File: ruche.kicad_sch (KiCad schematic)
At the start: 36 parts, among them IC2 MAX17048G+, IC3 L86-M33, IC4 SHT41-AD1B-R3, J13 Micro_SD_Card, U1 MKRWAN_1310, U2 MS5611-01BA, U3 XC6220B331MR

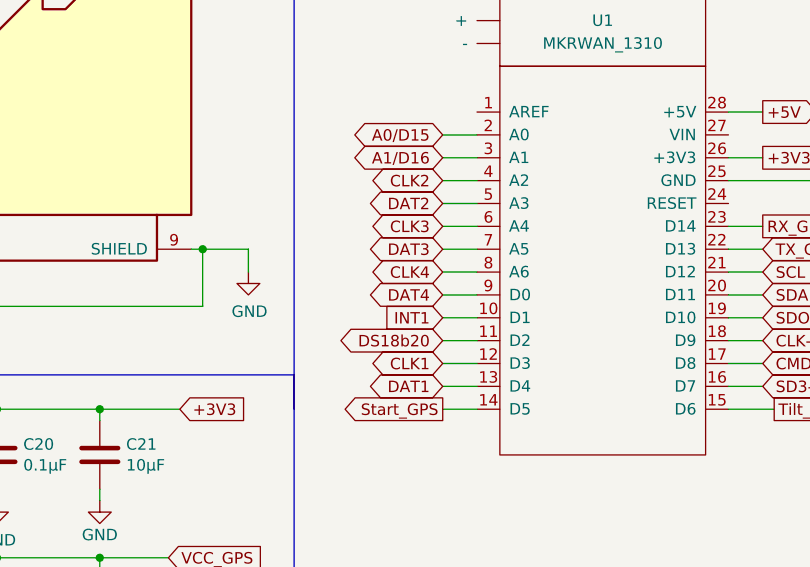
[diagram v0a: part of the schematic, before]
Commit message: Added HX711
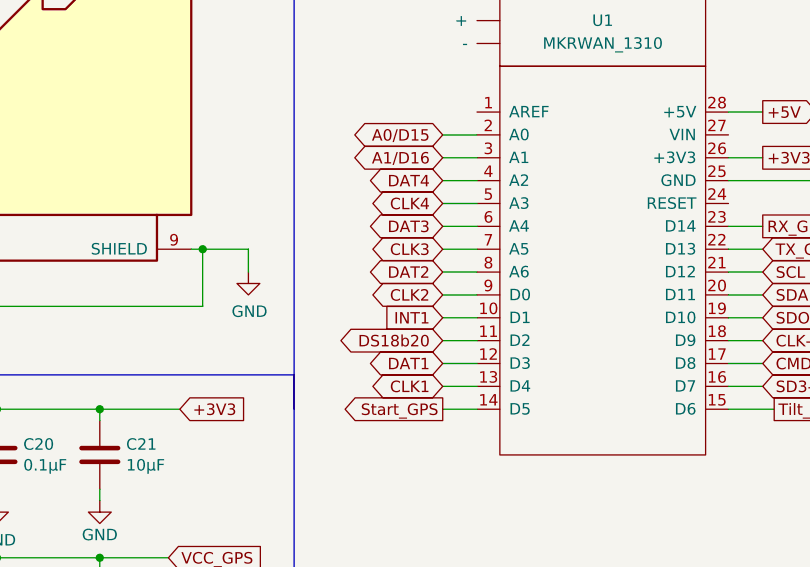
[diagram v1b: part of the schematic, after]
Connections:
- net CLK1: now also U1.13 (D4); no longer U1.12 (D3)
- net CLK2: now also U1.9 (D0); no longer U1.4 (A2)
- net CLK3: now also U1.7 (A5); no longer U1.6 (A4)
- net CLK4: now also U1.5 (A3); no longer U1.8 (A6)
- net DAT1: now also U1.12 (D3); no longer U1.13 (D4)
- net DAT2: now also U1.8 (A6); no longer U1.5 (A3)
- net DAT3: now also U1.6 (A4); no longer U1.7 (A5)
- net DAT4: now also U1.4 (A2); no longer U1.9 (D0)

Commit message: update
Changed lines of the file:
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@@
   (junction (at 53.34 72.39) (diameter 0) (color 0 0 0 0)
   )
-  (junction (at 191.77 91.44) (diameter 0) (color 0 0 0 0)
-  )
   (junction (at 220.98 78.74) (diameter 0) (color 0 0 0 0)
   )
@@
     (stroke (width 0) (type default) (color 0 0 0 0))
   )
+  (wire (pts (xy 191.77 88.9) (xy 191.77 93.98))
+    (stroke (width 0) (type default) (color 0 0 0 0))
+  )
   (wire (pts (xy 113.03 96.52) (xy 118.11 96.52))
     (stroke (width 0) (type default) (color 0 0 0 0))
@@
   )
   (wire (pts (xy 30.48 88.9) (xy 68.58 88.9))
-    (stroke (width 0) (type default) (color 0 0 0 0))
-  )
-  (wire (pts (xy 191.77 88.9) (xy 191.77 91.44))
     (stroke (width 0) (type default) (color 0 0 0 0))
   )
@@
     (pin "1")
   )
-  (symbol (lib_id "power:GND") (at 191.77 91.44 0) (unit 1)
-    (in_bom yes) (on_board yes)
-    (property "Reference" "#PWR0124" (id 0) (at 191.77 97.79 0)
-      (effects (font (size 1.27 1.27)) hide)
-    )
-    (property "Value" "GND" (id 1) (at 191.897 95.8342 0))
-    (property "Footprint" "" (id 2) (at 191.77 91.44 0)
-      (effects (font (size 1.27 1.27)) hide)
-    )
-    (property "Datasheet" "" (id 3) (at 191.77 91.44 0)
-      (effects (font (size 1.27 1.27)) hide)
-    )
-    (pin "1")
-  )
-  (symbol (lib_id "power:GND") (at 191.77 91.44 0) (unit 1)
-    (in_bom yes) (on_board yes)
-    (property "Reference" "#PWR0125" (id 0) (at 191.77 97.79 0)
-      (effects (font (size 1.27 1.27)) hide)
-    )
-    (property "Value" "GND" (id 1) (at 191.897 95.8342 0))
-    (property "Footprint" "" (id 2) (at 191.77 91.44 0)
-      (effects (font (size 1.27 1.27)) hide)
-    )
-    (property "Datasheet" "" (id 3) (at 191.77 91.44 0)
+  (symbol (lib_id "power:GND") (at 191.77 93.98 0) (unit 1)
+    (in_bom yes) (on_board yes)
+    (property "Reference" "#PWR0125" (id 0) (at 191.77 100.33 0)
+      (effects (font (size 1.27 1.27)) hide)
+    )
+    (property "Value" "GND" (id 1) (at 191.897 98.3742 0))
+    (property "Footprint" "" (id 2) (at 191.77 93.98 0)
+      (effects (font (size 1.27 1.27)) hide)
+    )
+    (property "Datasheet" "" (id 3) (at 191.77 93.98 0)
       (effects (font (size 1.27 1.27)) hide)
     )
@@
       (reference "#PWR0123") (unit 1) (value "GND") (footprint "")
     )
-    (path "/00000000-0000-0000-0000-000062832503"
-      (reference "#PWR0124") (unit 1) (value "GND") (footprint "")
-    )
     (path "/00000000-0000-0000-0000-000062832ae7"

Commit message: Update
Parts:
- added C51: 10µF, Capacitor_SMD:C_0603_1608Metric, symbol Device:C
- added C52: 0.1µF, Capacitor_SMD:C_0805_2012Metric, symbol Device:C
- added C53: 0.1µF, Capacitor_SMD:C_0603_1608Metric, symbol Device:C
- added C54: 10µF, Capacitor_SMD:C_0805_2012Metric, symbol Device:C
- added R41: 10K, Resistor_SMD:R_0603_1608Metric, symbol Device:R
- added U5: XC6220B331MR, Package_TO_SOT_SMD:SOT-23-5, symbol Regulator_Linear:XC6220B331MR
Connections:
- net +3V3: no longer C10.1, C12.1, C19.1, FB1.2, IC4.3 (VDD), J13.4 (VDD), R13.1, R14.1, R15.1
- net GND: now also C51.2, C52.2, C53.2, C54.2, U5.2 (GND)
- net VBAT: now also C51.1, C52.1, U5.1 (VIN)
- net A1/D16 renamed Start_modules
- net Start_modules: now also R41.2
- new net: R41.1, U5.3 (CE)
- new net VCC: C10.1, C12.1, C19.1, C53.1, C54.1, FB1.2, IC4.3 (VDD), J13.4 (VDD), R13.1, R14.1, R15.1, U5.5 (VOUT)
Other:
- note added: "Modules POWER SUPPLY"
- moved on the sheet: C15, C16, C17, C18, C5, FID1, FID2, FID3, FID4, IC2, R12, U1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

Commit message: Ajouté code
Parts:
- removed R12, R41: 10K, Resistor_SMD:R_0603_1608Metric, symbol Device:R
- added J19: Conn_01x02, Connector_JST:JST_PH_B2B-PH-K_1x02_P2.00mm_Vertical, symbol Connector_Generic:Conn_01x02
- C21: value 10µF -> 4.7µF
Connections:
- net GND: now also J19.2 (Pin_2)
- net Start_GPS: now also U3.3 (CE)
- net Start_modules: now also U5.3 (CE)
- net Reset-button: now reaches U1.24 (RESET)
- net Reset-button: now also J19.1 (Pin_1)
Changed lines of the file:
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@@
     (stroke (width 0) (type default) (color 0 0 0 0))
   )
+  (wire (pts (xy 146.05 176.53) (xy 146.05 182.88))
+    (stroke (width 0) (type default) (color 0 0 0 0))
+  )
   (wire (pts (xy 45.72 172.72) (xy 45.72 167.64))
     (stroke (width 0) (type default) (color 0 0 0 0))
@@
     (stroke (width 0) (type default) (color 0 0 0 0))
   )
-  (wire (pts (xy 55.88 29.21) (xy 54.61 29.21))
+  (wire (pts (xy 54.61 29.21) (xy 63.5 29.21))
     (stroke (width 0) (type default) (color 0 0 0 0))
   )
@@
     (stroke (width 0) (type default) (color 0 0 0 0))
   )
+  (wire (pts (xy 140.97 173.99) (xy 153.67 173.99))
+    (stroke (width 0) (type default) (color 0 0 0 0))
+  )
   (wire (pts (xy 266.7 105.41) (xy 266.7 106.68))
     (stroke (width 0) (type default) (color 0 0 0 0))
@@
     (stroke (width 0) (type default) (color 0 0 0 0))
   )
+  (wire (pts (xy 172.72 49.53) (xy 176.53 49.53))
+    (stroke (width 0) (type default) (color 0 0 0 0))
+  )
   (wire (pts (xy 88.9 167.64) (xy 91.44 167.64))
     (stroke (width 0) (type default) (color 0 0 0 0))
@@
     (stroke (width 0) (type default) (color 0 0 0 0))
   )
+  (wire (pts (xy 153.67 176.53) (xy 146.05 176.53))
+    (stroke (width 0) (type default) (color 0 0 0 0))
+  )
   (wire (pts (xy 30.48 162.56) (xy 49.53 162.56))
     (stroke (width 0) (type default) (color 0 0 0 0))
@@
     (stroke (width 0) (type default) (color 0 0 0 0))
   )
-  (wire (pts (xy 53.34 172.72) (xy 49.53 172.72))
-    (stroke (width 0) (type default) (color 0 0 0 0))
-  )
-  (wire (pts (xy 60.96 172.72) (xy 63.5 172.72))
+  (wire (pts (xy 49.53 172.72) (xy 63.5 172.72))
     (stroke (width 0) (type default) (color 0 0 0 0))
   )
@@
     )
   )
+  (global_label "Reset-button" (shape input) (at 140.97 173.99 180) (fields_autoplaced)
+    (effects (font (size 1.27 1.27)) (justify right))
+    (property "Intersheet References" "${INTERSHEET_REFS}" (id 0) (at 125.8248 173.9106 0)
+      (effects (font (size 1.27 1.27)) (justify right) hide)
+    )
+  )
   (global_label "+3V3" (shape input) (at 110.49 114.3 0) (fields_autoplaced)
     (effects (font (size 1.27 1.27)) (justify left))
@@
     )
   )
+  (global_label "Reset-button" (shape output) (at 176.53 49.53 0) (fields_autoplaced)
+    (effects (font (size 1.27 1.27)) (justify left))
+    (property "Intersheet References" "${INTERSHEET_REFS}" (id 0) (at 191.6752 49.4506 0)
+      (effects (font (size 1.27 1.27)) (justify left) hide)
+    )
+  )
   (global_label "DAT1" (shape bidirectional) (at 140.97 67.31 180) (fields_autoplaced)
     (effects (font (size 1.27 1.27)) (justify right))
@@
     )
   )
-  (symbol (lib_id "Device:R") (at 59.69 29.21 270) (unit 1)
+  (symbol (lib_id "power:GND") (at 146.05 182.88 0) (unit 1)
     (in_bom yes) (on_board yes)
-    (property "Reference" "R41" (id 0) (at 59.69 22.6822 90))
-    (property "Value" "10K" (id 1) (at 59.69 26.2636 90))
-    (property "Footprint" "Resistor_SMD:R_0603_1608Metric" (id 2) (at 59.69 27.432 90)
+    (property "Reference" "#PWR0202" (id 0) (at 146.05 189.23 0)
+      (effects (font (size 1.27 1.27)) hide)
+    )
+    (property "Value" "GND" (id 1) (at 146.177 187.2742 0))
+    (property "Footprint" "" (id 2) (at 146.05 182.88 0)
       (effects (font (size 1.27 1.27)) hide)
     )
-    (property "Datasheet" "~" (id 3) (at 59.69 29.21 0)
+    (property "Datasheet" "" (id 3) (at 146.05 182.88 0)
       (effects (font (size 1.27 1.27)) hide)
     )
     (pin "1")
-    (pin "2")
   )
   (symbol (lib_id "Device:C") (at 232.41 83.82 0) (unit 1)
@@
       (effects (font (size 1.27 1.27)) (justify left))
     )
-    (property "Value" "10µF" (id 1) (at 104.521 120.523 0)
+    (property "Value" "4.7µF" (id 1) (at 104.521 120.523 0)
       (effects (font (size 1.27 1.27)) (justify left))
     )
@@
     (pin "2")
   )
-  (symbol (lib_id "Device:R") (at 57.15 172.72 270) (unit 1)
-    (in_bom yes) (on_board yes)
-    (property "Reference" "R12" (id 0) (at 57.15 166.1922 90))
-    (property "Value" "10K" (id 1) (at 57.15 169.7736 90))
-    (property "Footprint" "Resistor_SMD:R_0603_1608Metric" (id 2) (at 57.15 170.942 90)
-      (effects (font (size 1.27 1.27)) hide)
-    )
-    (property "Datasheet" "~" (id 3) (at 57.15 172.72 0)
-      (effects (font (size 1.27 1.27)) hide)
-    )
-    (pin "1")
-    (pin "2")
-  )
   (symbol (lib_id "Device:R") (at 31.75 66.04 0) (unit 1)
     (in_bom yes) (on_board yes)
@@
     (pin "5")
   )
+  (symbol (lib_id "Connector_Generic:Conn_01x02") (at 158.75 173.99 0) (unit 1)
+    (in_bom yes) (on_board yes)
+    (property "Reference" "J19" (id 0) (at 160.782 174.1932 0)
+      (effects (font (size 1.27 1.27)) (justify left))
+    )
+    (property "Value" "Conn_01x02" (id 1) (at 160.782 176.5046 0)
+      (effects (font (size 1.27 1.27)) (justify left))
+    )
+    (property "Footprint" "Connector_JST:JST_PH_B2B-PH-K_1x02_P2.00mm_Vertical" (id 2) (at 158.75 173.99 0)
+      (effects (font (size 1.27 1.27)) hide)
+    )
+    (property "Datasheet" "~" (id 3) (at 158.75 173.99 0)
+      (effects (font (size 1.27 1.27)) hide)
+    )
+    (pin "1")
+    (pin "2")
+  )
   (symbol (lib_id "Device:C") (at 90.17 33.02 0) (unit 1)
     (in_bom yes) (on_board yes)
@@
       (reference "#PWR0136") (unit 1) (value "GND") (footprint "")
     )
-    (path "/00000000-0000-0000-0000-0000609e7af1/f314badf-692d-404c-b7d4-9383e3c1a0d7"
-      (reference "#PWR0137") (unit 1) (value "GND") (footprint "")
-    )
     (path "/c5a9172d-5cdb-4b78-b75d-3b37a039f7ea/f9fee2cc-fac7-443b-971c-536031ac3773"
       (reference "#PWR0138") (unit 1) (value "GND") (footprint "")
@@
       (reference "#PWR0201") (unit 1) (value "GND") (footprint "")
     )
+    (path "/34ea9698-2f06-4c4a-87a4-bceed7fb1035"
+      (reference "#PWR0202") (unit 1) (value "GND") (footprint "")
+    )
+    (path "/00000000-0000-0000-0000-0000609e7af1/f314badf-692d-404c-b7d4-9383e3c1a0d7"
+      (reference "#PWR0204") (unit 1) (value "GND") (footprint "")
+    )
     (path "/00000000-0000-0000-0000-0000609e7af1/27949037-10e0-465d-ad1e-4223c09881c0"
       (reference "C1") (unit 1) (value "100µF/35V") (footprint "Capacitor_SMD:CP_Elec_6.3x7.7")
@@
     )
     (path "/945b8470-7757-4ab2-b2d6-a58413988c3e"
-      (reference "C21") (unit 1) (value "10µF") (footprint "Capacitor_SMD:C_0805_2012Metric")
+      (reference "C21") (unit 1) (value "4.7µF") (footprint "Capacitor_SMD:C_0805_2012Metric")
     )
     (path "/c5a9172d-5cdb-4b78-b75d-3b37a039f7ea/013812a3-dc9e-458a-8547-ba7ef54622c5"
@@
       (reference "J18") (unit 1) (value "Conn_01x04") (footprint "Connector_JST:JST_PH_B4B-PH-K_1x04_P2.00mm_Vertical")
     )
+    (path "/cb3195ff-5ba9-4060-a8cd-a6a427bc1dc8"
+      (reference "J19") (unit 1) (value "Conn_01x02") (footprint "Connector_JST:JST_PH_B2B-PH-K_1x02_P2.00mm_Vertical")
+    )
     (path "/00000000-0000-0000-0000-00006011445d/79fe9980-abb4-43ab-a32a-a54b421cb267"
       (reference "JP1") (unit 1) (value "SolderJumper_3_Open") (footprint "Jumper:SolderJumper-3_P1.3mm_Open_RoundedPad1.0x1.5mm_NumberLabels")
@@
       (reference "R11") (unit 1) (value "10K") (footprint "Resistor_SMD:R_0603_1608Metric")
     )
-    (path "/bb1ede6c-c90f-4449-b20d-4fa8739db41b"
-      (reference "R12") (unit 1) (value "10K") (footprint "Resistor_SMD:R_0603_1608Metric")
-    )
     (path "/c40fa437-6b2b-4bf8-8fed-591cab698a11"
       (reference "R13") (unit 1) (value "10k") (footprint "Resistor_SMD:R_0603_1608Metric")
@@
       (reference "R40") (unit 1) (value "10K") (footprint "Resistor_SMD:R_0603_1608Metric")
     )
-    (path "/2df4a7bf-fc01-497a-8f52-9fba9e76ef75"
-      (reference "R41") (unit 1) (value "10K") (footprint "Resistor_SMD:R_0603_1608Metric")
-    )
     (path "/00000000-0000-0000-0000-000062773850"
